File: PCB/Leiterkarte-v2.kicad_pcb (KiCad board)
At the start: 4 copper layers, 40.3 x 85.7 mm, 55 parts

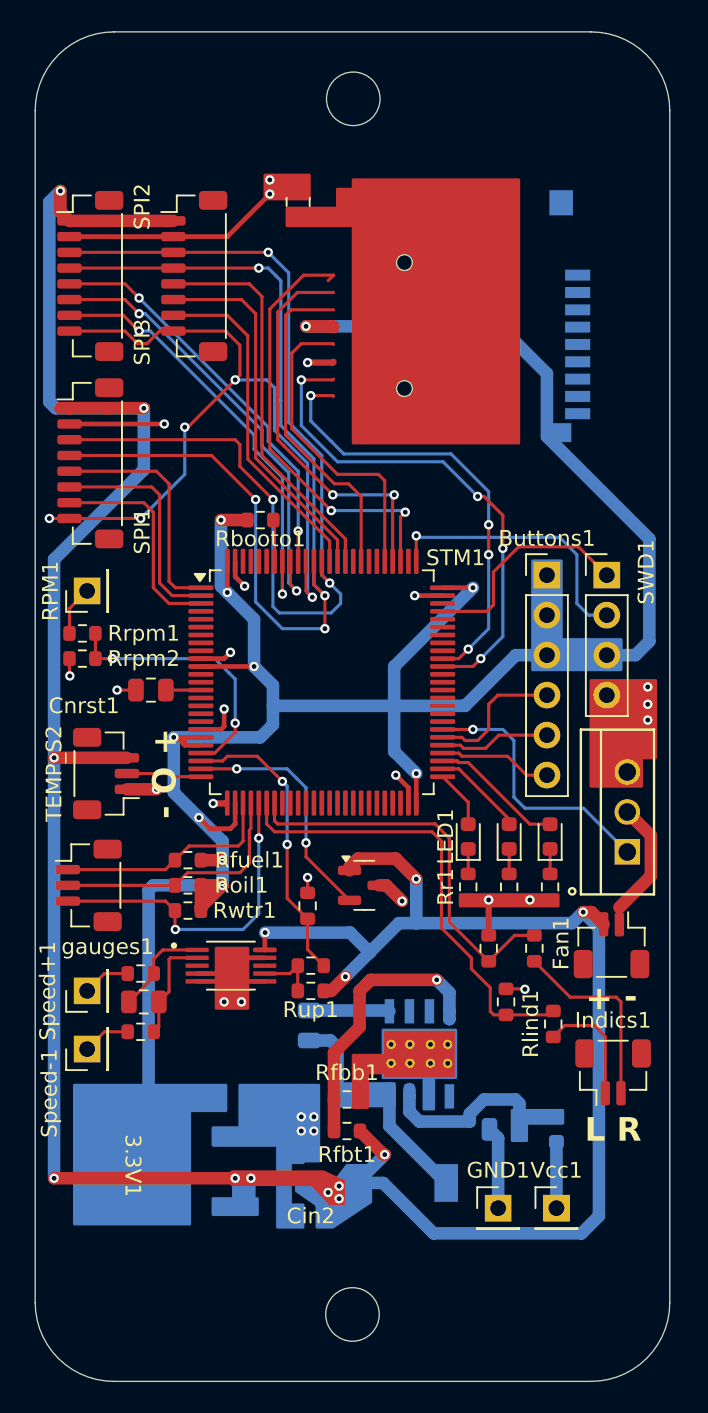
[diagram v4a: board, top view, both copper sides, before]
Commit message: Added ground pours
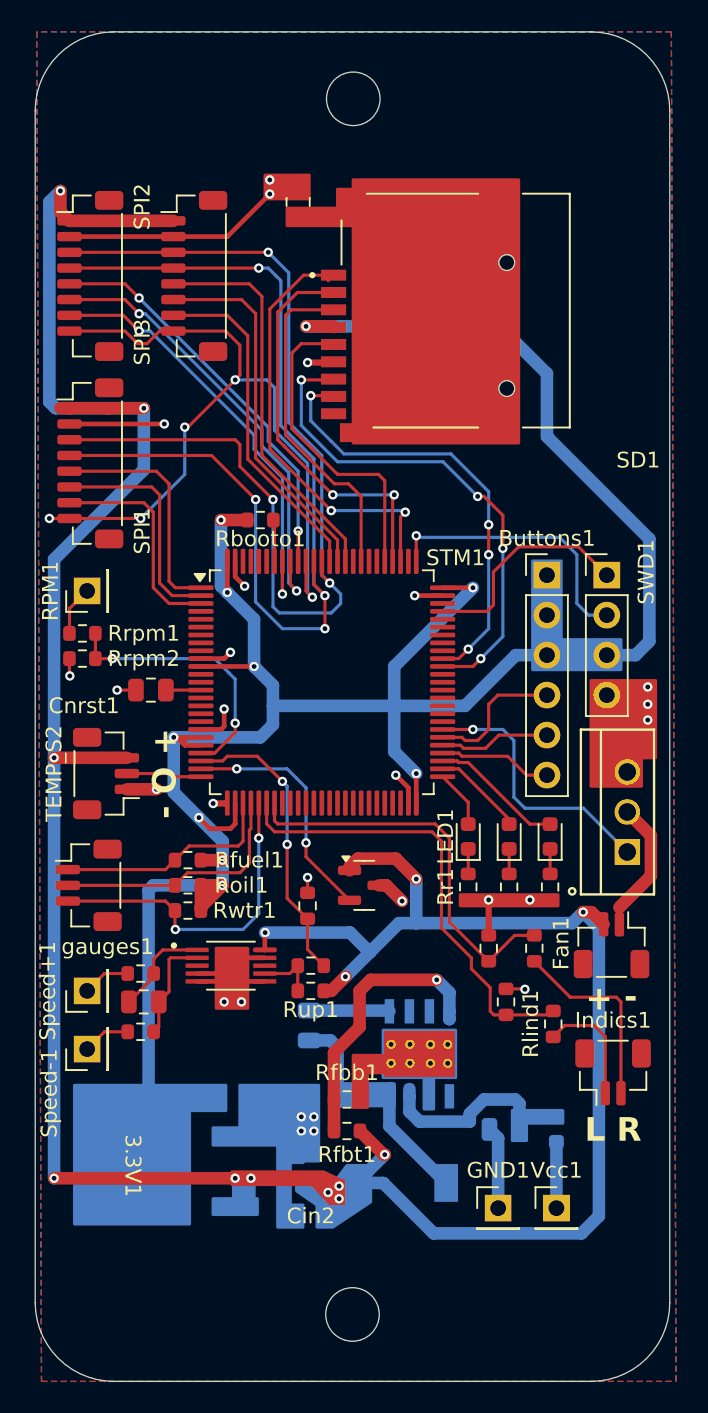
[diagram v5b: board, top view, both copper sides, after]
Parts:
- SD1: moved to F.Cu
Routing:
- net GND: track 60.2 -> 67.4 mm
- added copper zone on B.Cu, net GND
- added copper zone on F.Cu, net GND

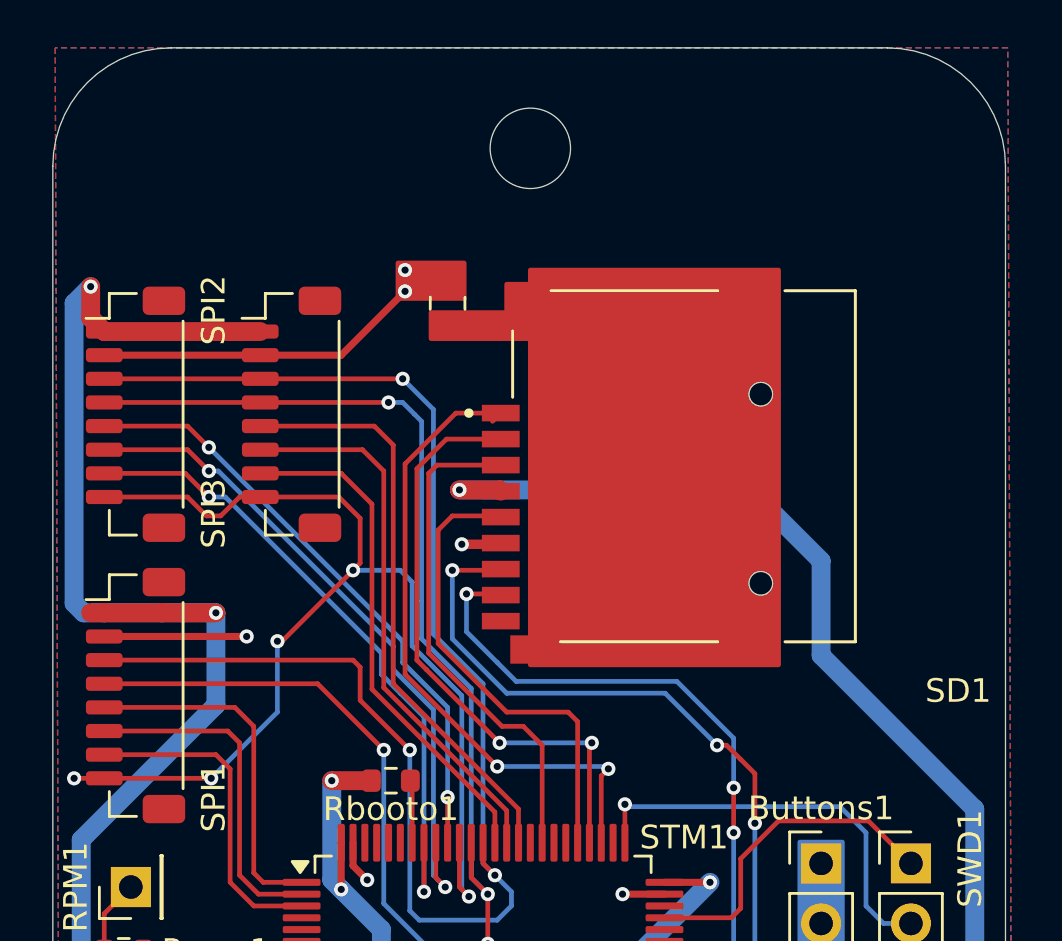
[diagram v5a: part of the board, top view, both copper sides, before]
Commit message: Added 3D models for the JST connectors, MSD-1-A, MOSFET and MAX9924
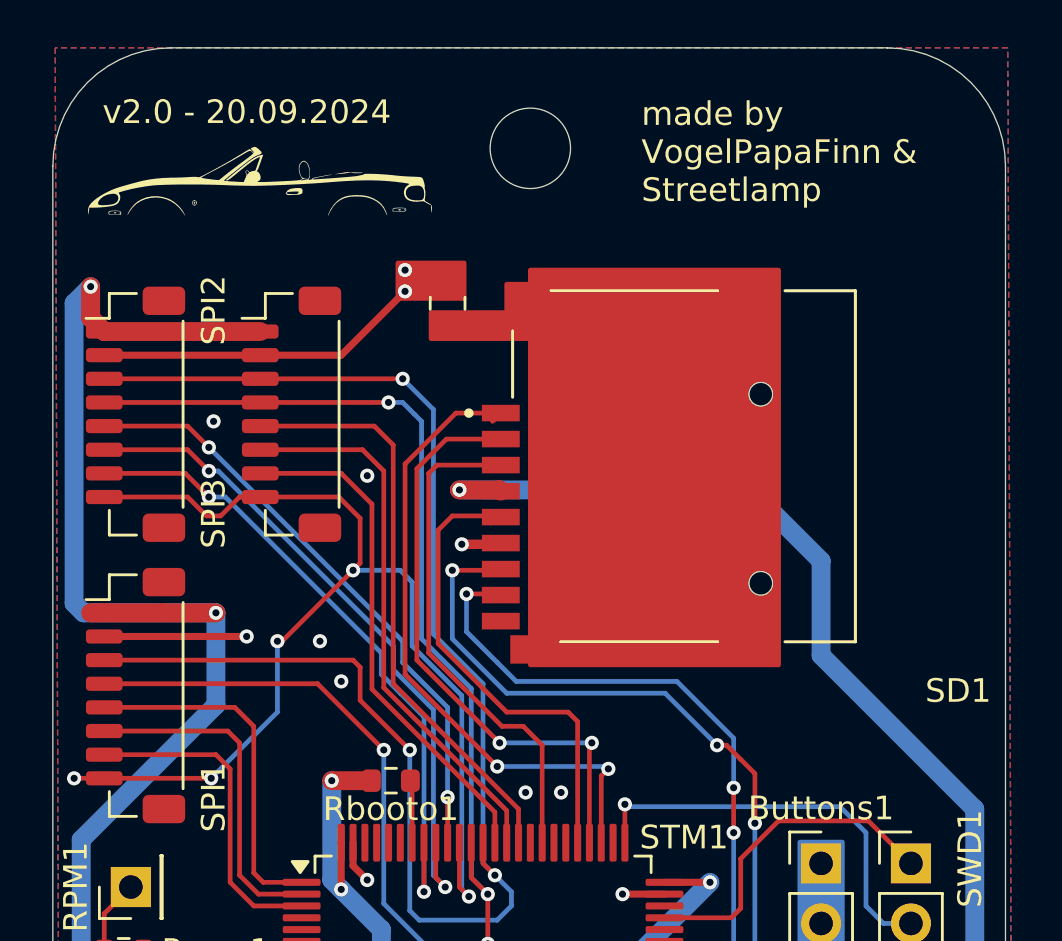
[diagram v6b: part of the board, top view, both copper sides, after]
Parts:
- added G***: LOGO, Images:mx5, F.Cu at (153.2, 53.6)
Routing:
- net GND: vias 27 -> 33
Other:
- board text added: "made by VogelPapaFinn & Streetlamp"
- board text added: "v2.0 - 20.09.2024"

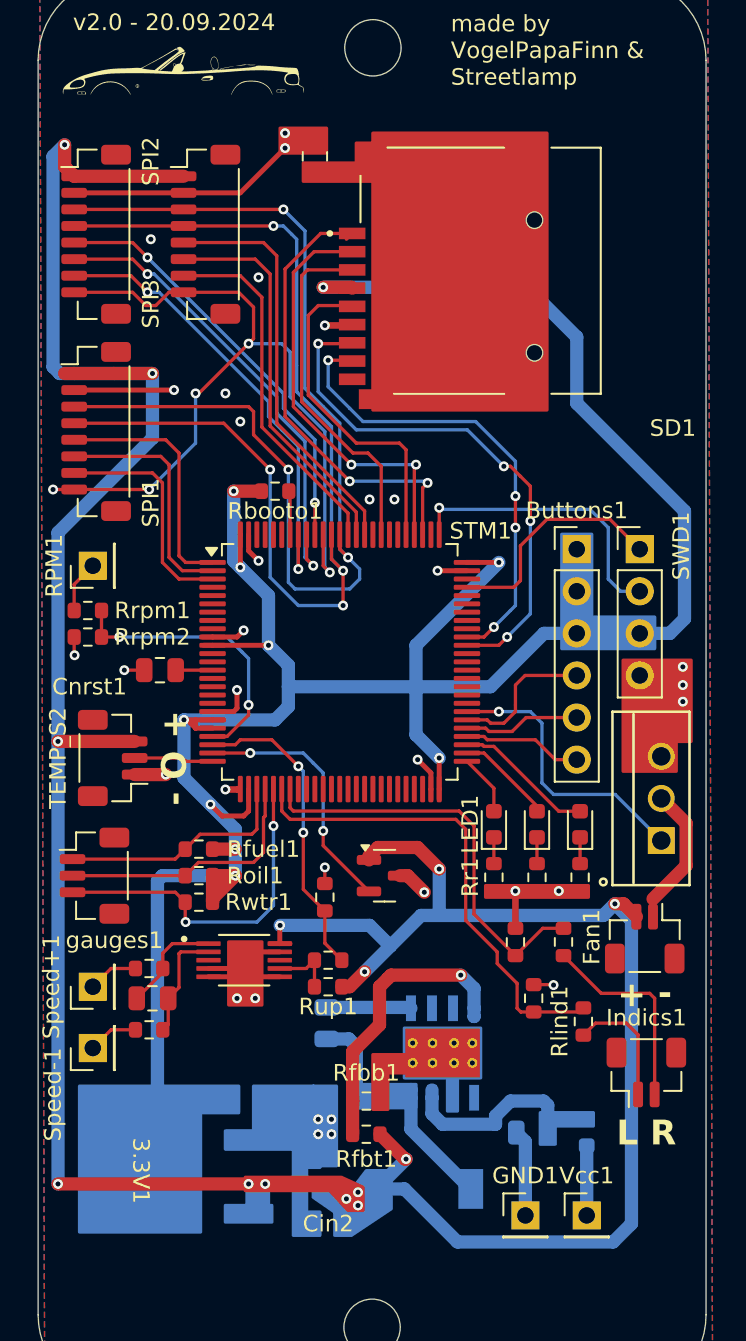
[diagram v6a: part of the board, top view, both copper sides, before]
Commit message: Moved component names on the PCB name; Rotated MOSFET
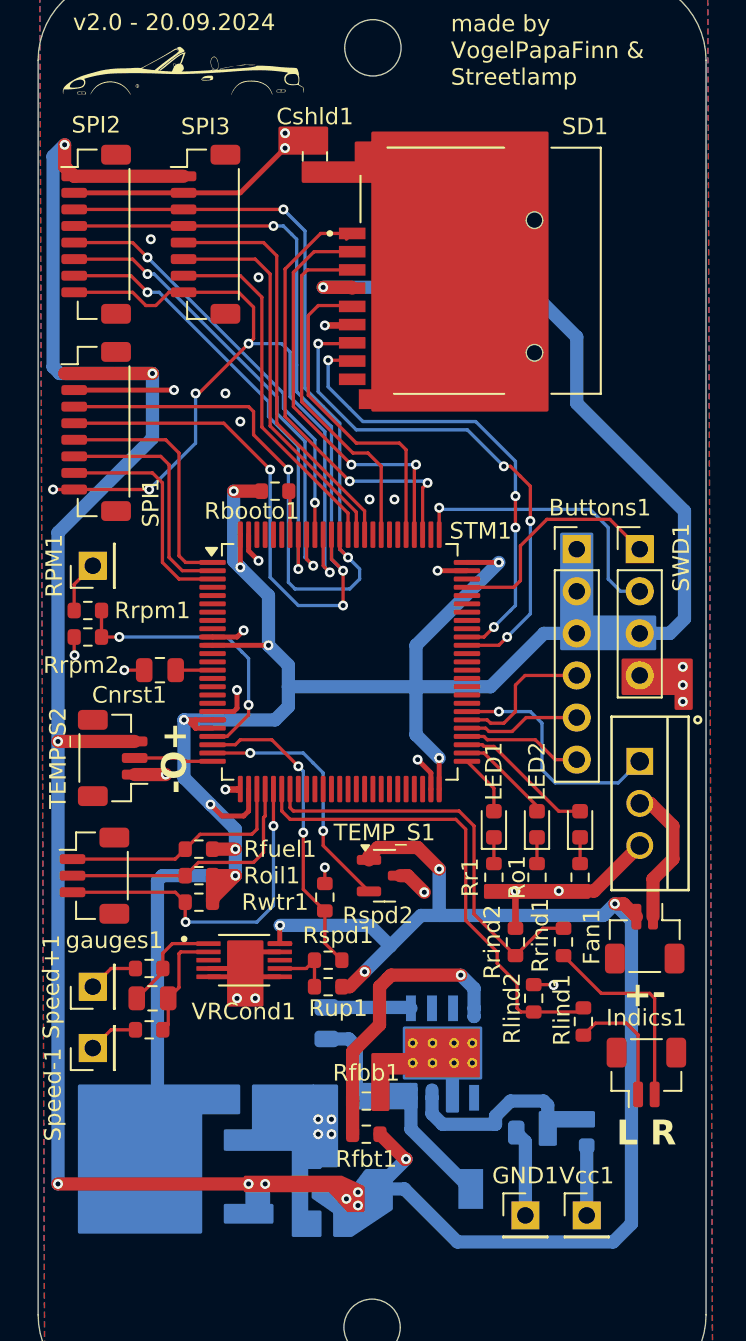
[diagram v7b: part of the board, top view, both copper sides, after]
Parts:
- moved Ufan1 4.95 mm to (180.7, 95.8), turned to -90 degrees
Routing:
- net GND: track 67.4 -> 72.1 mm
- net FANCTRL: track 17.1 -> 14.4 mm
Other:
- board text added: "-+"
- board text added: "-O+"
- board text added: "FOW"
- board text removed: "- +"
- board text removed: "- O +"
- board text removed: "F O W"

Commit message: Replaced Inductor L1; Replaced MOSFET; Places some vias in the ground pours
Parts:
- removed Ufan1: IRL540NPBF, IRL540NPBF:PG-TO220-3_INF
- added Qfan1: 2N7002-HXY, Package_TO_SOT_SMD:SOT-23, F.Cu at (180.0, 101.9)
- L1: footprint Inductor_SMD:L_6.3x6.3_H3 -> FXL0630-1R5-M:INDM7066X300N
- moved Cin2 2.22 mm to (160.5, 121.9), turned to 90 degrees
- moved Cout2 1.70 mm to (162.9, 121.9)
- moved L1 1.30 mm to (167.7, 122.9), turned to -90 degrees
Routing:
- net Net-(Fan1-Pin_1): track 8.54 -> 0.00 mm
- net GND: track 72.1 -> 67.4 mm, vias 33 -> 44
- net Net-(5V1-PH): track 12.6 -> 9.92 mm
- net FANCTRL: track 14.4 -> 15.7 mm, vias 1 -> 2
- net +5V: track 180.5 -> 180.4 mm, vias 14 -> 12
